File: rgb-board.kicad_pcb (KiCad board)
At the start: 2 copper layers, 178 x 129.5 mm, 87 parts, among them J1 Conn_02x25_Odd_Even, J10 Conn_Coaxial, J11 Conn_Coaxial, J2 SCART-F, J3 TEST_1P, J4 TEST_1P, J5 DE15_Plug_HighDensity_Mountin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, K1 G6K-2PY-12DC, Q101 BC850C, Q105 BC850C, Q109 BC850C, Q113 BC850C, Q114 BC850C, Q201 BC850C, SW1 SW_DPDT_x2, SW2 SPUJ193700, U1 NCP1117-12_SOT223

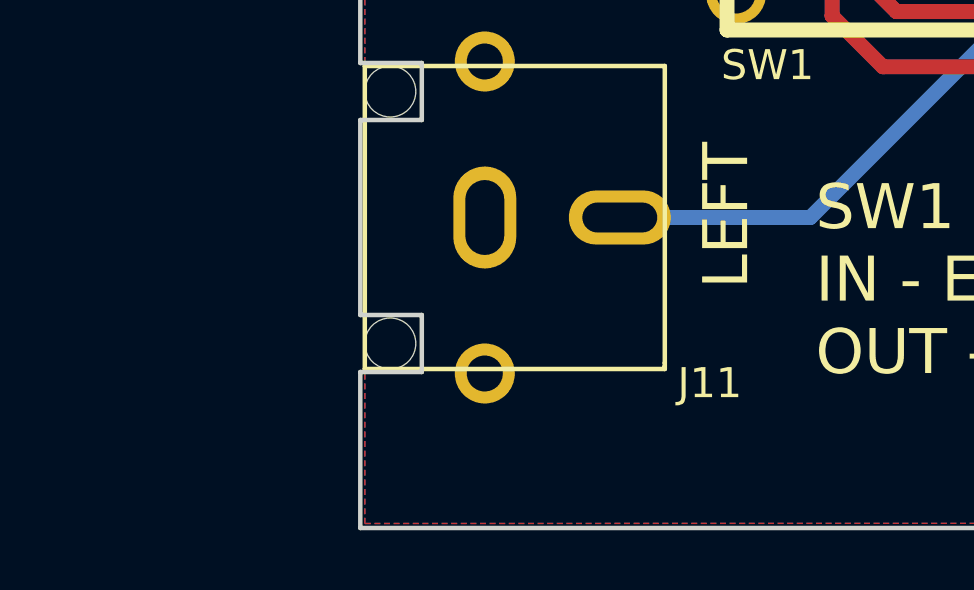
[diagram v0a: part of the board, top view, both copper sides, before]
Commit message: Add CUI Devices / SAME SKY Devices SJ1-353XNG Series Audio Jack 3.5 mm Female.
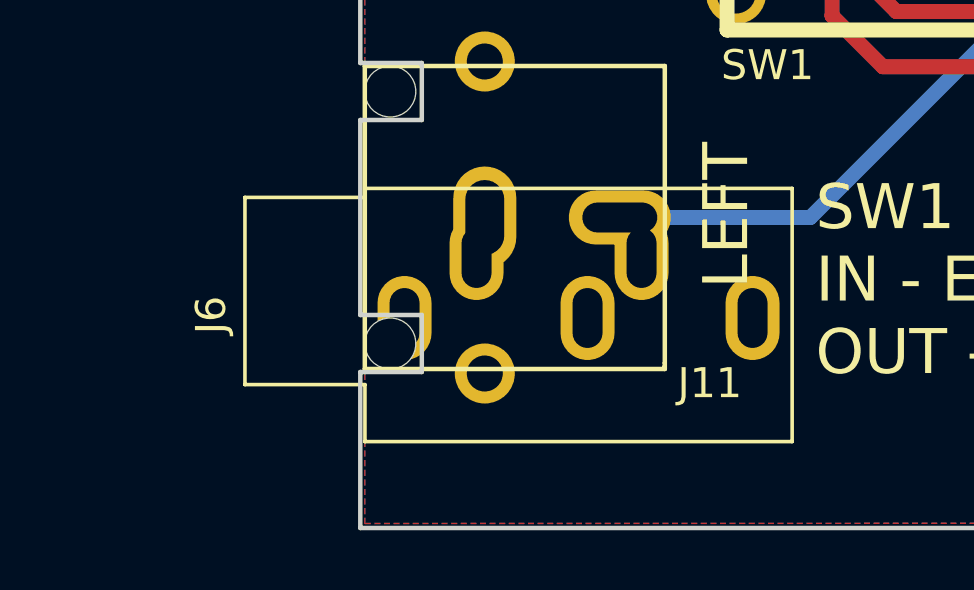
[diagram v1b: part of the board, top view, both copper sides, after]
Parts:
- added J6: SJ1-3535NG, Connector_Audio:Jack_3.5mm_CUI_SJ1-3535NG_Horizontal, F.Cu at (51.3, 152.9)

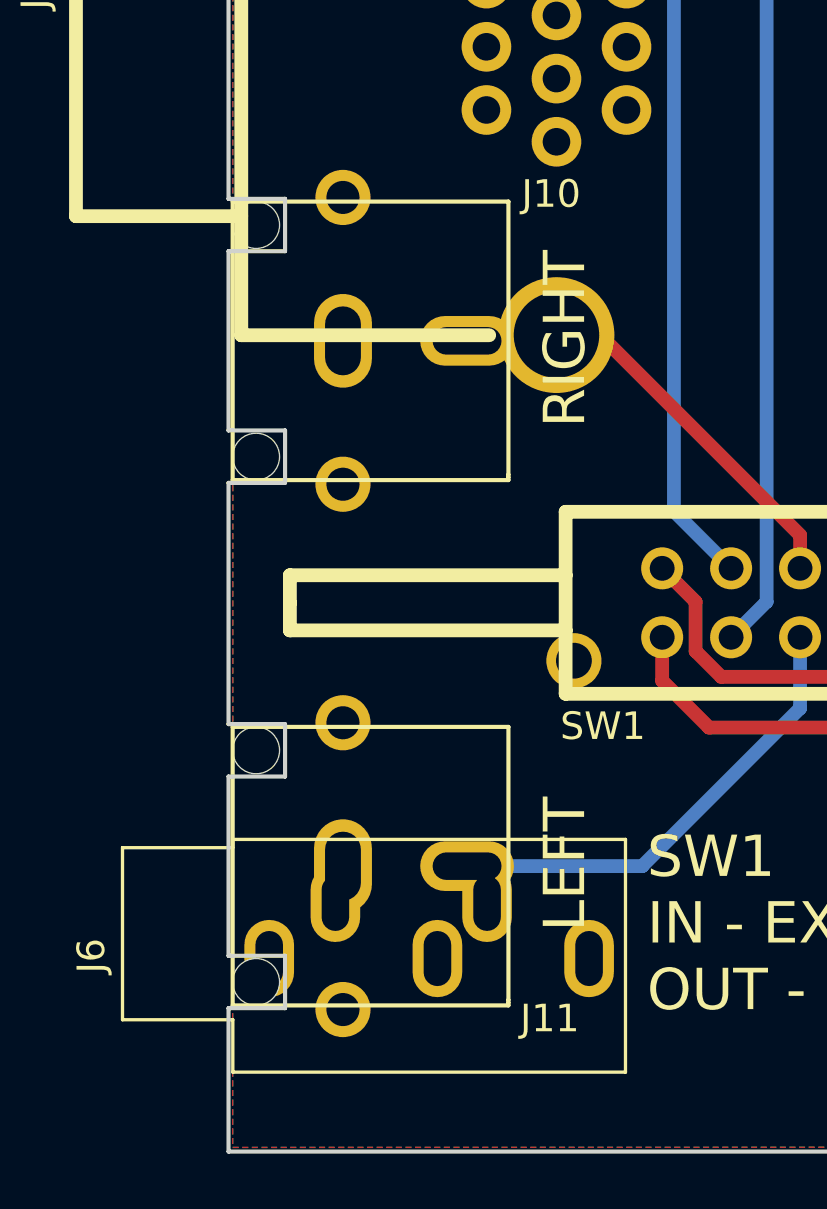
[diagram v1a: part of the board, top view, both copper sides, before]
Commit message: Remove audio RCA connectors.
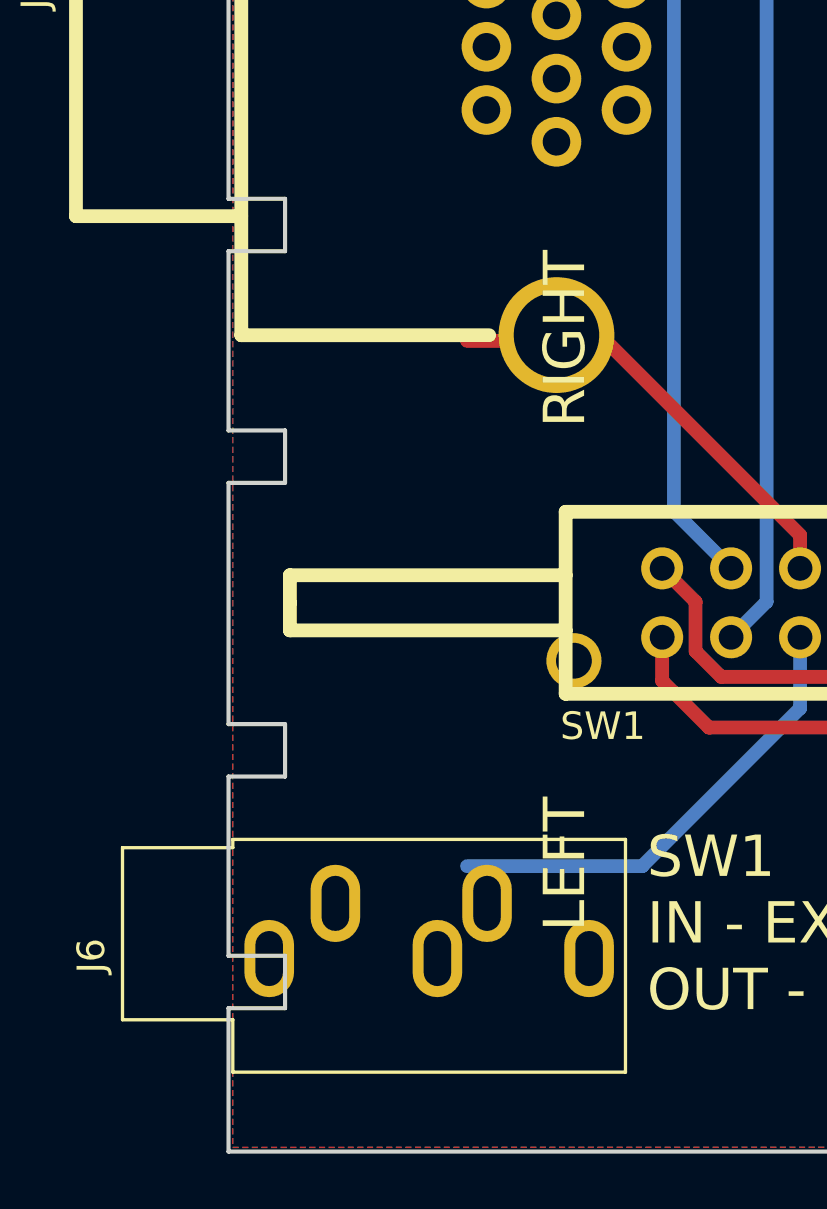
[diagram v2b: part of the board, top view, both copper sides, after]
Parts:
- removed J10, J11: Conn_Coaxial, rcj-41x:RCJ-04X

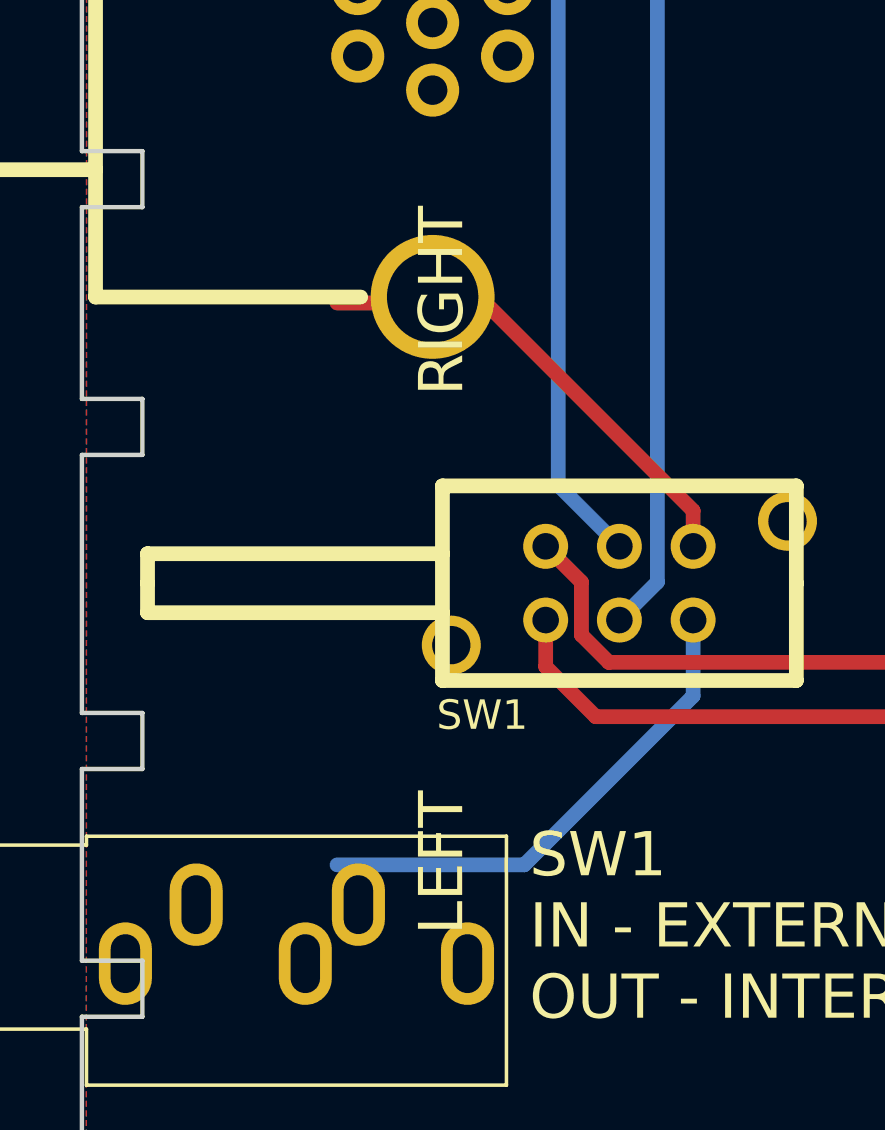
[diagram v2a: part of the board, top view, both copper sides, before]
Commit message: Remove audio RCA connectors.
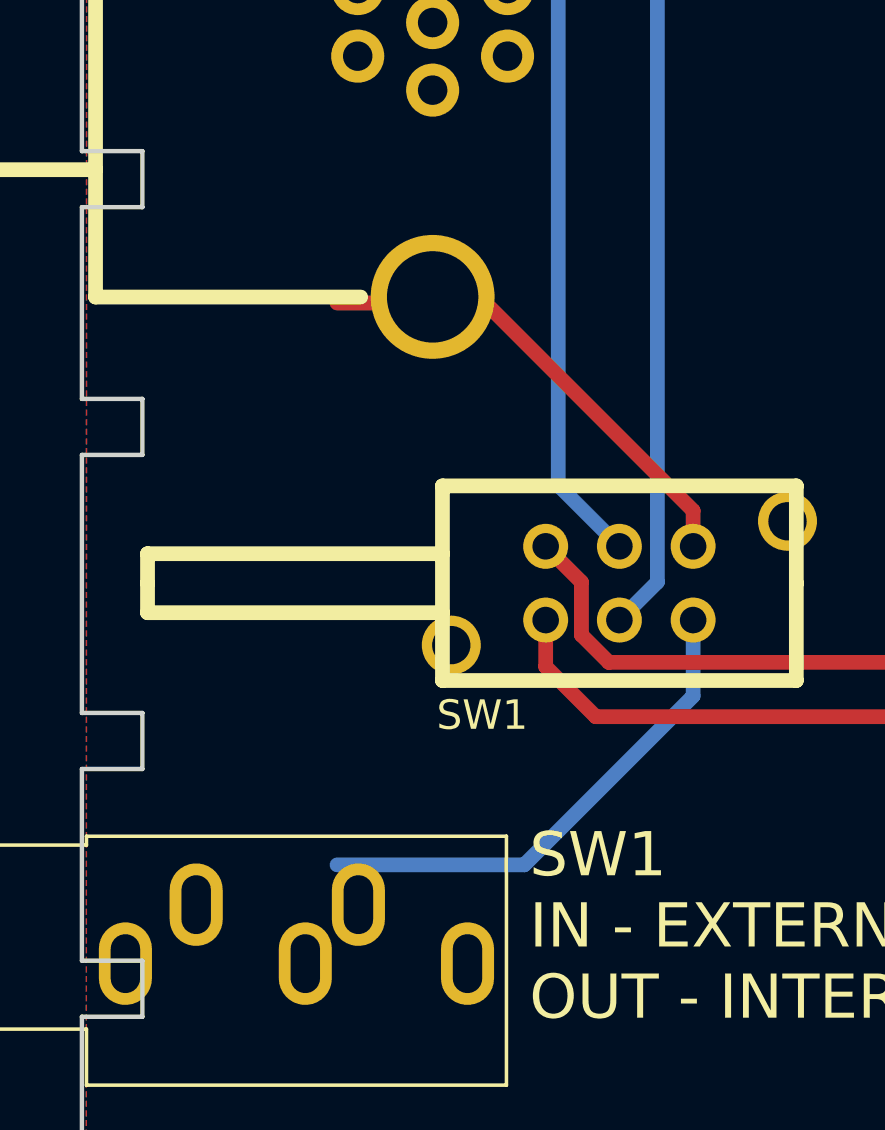
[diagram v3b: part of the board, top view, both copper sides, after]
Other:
- board text removed: "LEFT"
- board text removed: "RIGHT"
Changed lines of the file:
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@@
-		)
-	)
-	(gr_text "RIGHT"
-		(at 62.025 130.425 90)
-		(layer "F.SilkS")
-		(effects
-			(font
-				(size 1.5 1.5)
-				(thickness 0.3)
-			)
-		)
-	)
-	(gr_text "LEFT"
-		(at 62.025 149.475 90)
-		(layer "F.SilkS")
-		(effects
-			(font
-				(size 1.5 1.5)
-				(thickness 0.3)
-			)
 		)
 	)
